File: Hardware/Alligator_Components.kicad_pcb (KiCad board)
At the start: 2 copper layers, 60 x 110 mm, 109 parts, among them J1 SWD_Header, J2 Eurorack_10_pin_power, J3 Conn_01x08_Female, J4 Conn_01x08_Female, J5 Conn_01x08_Female, J6 Conn_01x08_Female, U1 STM32H743ZITx, U2 IS42S16400J-xC, U3 PCM5100APW, U4 SSI2164, U5 MCP6004, U6 MCP6004, U7 TL074, U8 LM1117-3.3, Y1 8MHz 20pF

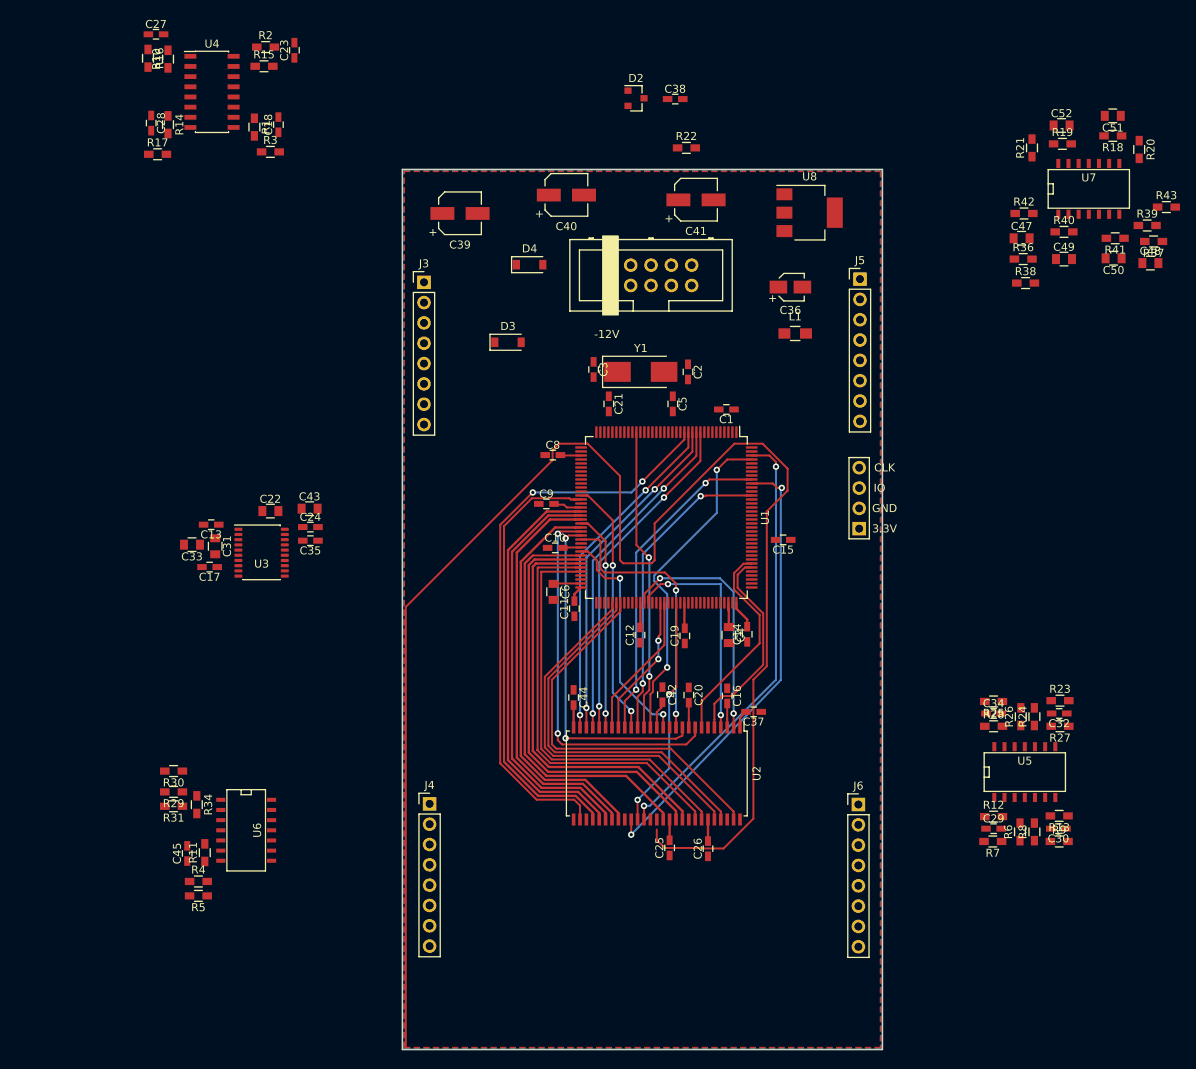
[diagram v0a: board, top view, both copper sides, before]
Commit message: Further routing of PCB
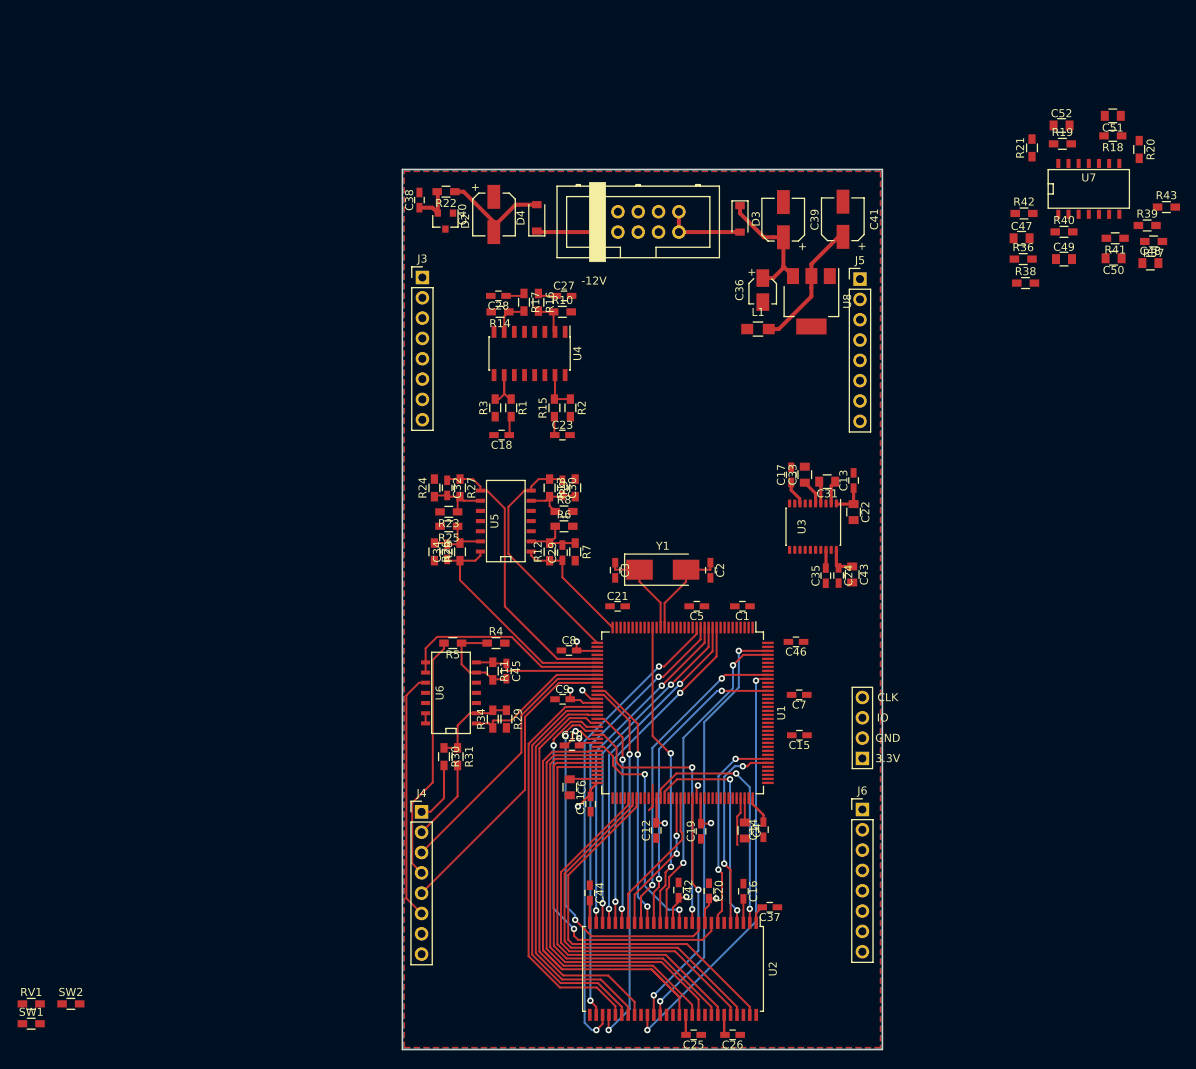
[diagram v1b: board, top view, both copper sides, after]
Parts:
- added C46: 100nF, Capacitors_SMD:C_0603_HandSoldering, F.Cu at (149.2, 109.0)
- added C7: 100nF, Capacitors_SMD:C_0603_HandSoldering, F.Cu at (149.6, 115.7)
- added RV1: A10k, Resistors_SMD:R_0603_HandSoldering, F.Cu at (53.6, 154.3)
- added SW1: SW_SPST, Resistors_SMD:R_0603_HandSoldering, F.Cu at (53.6, 156.8)
- added SW2: SW_SPDT_MSM, Resistors_SMD:R_0603_HandSoldering, F.Cu at (58.6, 154.3)
- moved C32 81.5 mm to (105.6, 89.8), turned to 270 degrees
- moved R27 80.7 mm to (107.2, 89.8), turned to 270 degrees
- moved C13 80.5 mm to (156.4, 88.9), turned to 90 degrees
- moved R24 80.3 mm to (104.0, 89.8)
- moved R23 80.0 mm to (105.8, 92.8), turned to 180 degrees
- moved C33 77.1 mm to (150.3, 88.2), turned to 90 degrees
- moved C31 76.9 mm to (153.1, 89.0), turned to 180 degrees
- moved R26 76.1 mm to (104.0, 97.8), turned to 270 degrees
- moved R13 75.8 mm to (118.4, 89.8), turned to 270 degrees
- moved C30 75.2 mm to (120.0, 89.8), turned to 270 degrees
- moved R9 74.9 mm to (121.6, 89.8), turned to 90 degrees
- moved C17 73.6 mm to (148.6, 88.2), turned to 90 degrees
- moved C22 72.9 mm to (156.4, 92.8), turned to 270 degrees
- moved U5 72.1 mm to (112.8, 94.0), turned to 90 degrees
- moved R25 71.5 mm to (105.8, 94.6)
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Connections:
- J3 pad 2: /MODE1 -> /EXT_AUDIO_IN_L
- J3 pad 3: /MODE2 -> /EXT_AUDIO_IN_R
- J3 pad 4: /USB_VBUS -> /RESET
- J3 pad 5: /USB_DM -> /DELAY_CV_L
- J3 pad 6: /USB_DP -> /DELAY_CV_R
- J4 pad 1: /EXT_AUDIO_IN_L -> /MIX_CV
- J4 pad 2: /EXT_AUDIO_IN_R -> /MIX_POT
- J4 pad 3: /RESET -> /FEEDBACK_POT
- J4 pad 4: /EXT_AUDIO_OUT_L -> /FEEDBACK_CV
- J4 pad 5: /EXT_AUDIO_OUT_R -> /DELAY_POT_L
- J5 pad 1: /DELAY_CV_L -> /EXT_AUDIO_OUT_L
- J5 pad 2: /DELAY_POT_L -> /EXT_AUDIO_OUT_R
- J5 pad 3: /DELAY_CV_R -> /DELAY_POT_R
- J5 pad 4: /DELAY_POT_R -> /ADC12_INP7_PA7
- J5 pad 5: /ADC12_INP7_PA7 -> /ADC12_INP14_PA2
- J5 pad 6: /ADC12_INP14_PA2 -> /MODE1
- J5 pad 7: GND -> /MODE2
- J5 pad 8: +3.3VA -> Net-(J5-Pad8)
- J6 pad 1: /MIX_POT -> /LED1
- J6 pad 2: /MIX_CV -> /LED2
- J6 pad 3: /FEEDBACK_CV -> /USB_VBUS
- J6 pad 4: /FEEDBACK_POT -> /USB_DM
- J6 pad 5: /LED1 -> /USB_DP
- J6 pad 6: /LED2 -> Net-(J6-Pad6)
- U1 pad 117: Net-(U1-Pad117) -> /DAC_BCLK
- U1 pad 27: /AUDIO_IN_R -> /MIX_WET_CTL
- U1 pad 29: Net-(U1-Pad29) -> /DAC_DATA
- U1 pad 34: /DELAY_CV_R -> /MIX_DRY_CTL
- U1 pad 36: Net-(U1-Pad36) -> /AUDIO_IN_L
- U1 pad 37: /DELAY_CV_SCALED_L -> /AUDIO_IN_R
- U1 pad 40: /MIX_DRY_CTL -> Net-(U1-Pad40)
- U1 pad 41: /MIX_WET_CTL -> /DELAY_CV_SCALED_L
- U1 pad 42: /AUDIO_IN_L -> /DELAY_CV_SCALED_R
- U1 pad 43: /FEEDBACK_CV_SCALED -> /CLOCK_SCALED
- U1 pad 44: /DELAY_CV_SCALED_R -> /FEEDBACK_CV_SCALED
- U1 pad 45: /DELAY_POT_L -> /WET_DRY_MIX
- U1 pad 47: /WET_DRY_MIX -> /DELAY_POT_L
- U1 pad 69: /DAC_BCLK -> Net-(U1-Pad69)
- U1 pad 76: /DAC_DATA -> Net-(U1-Pad76)
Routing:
- net (no net): track 195.2 -> 0.00 mm
- net /FMC_A5: track 0.00 -> 59.7 mm, vias 0 -> 2
- net /DELAY_POT_L: track 0.00 -> 38.2 mm
- net /DELAY_CV_SCALED_L: track 0.00 -> 35.6 mm
- net /FEEDBACK_POT: track 0.00 -> 33.7 mm
- net /CLOCK: track 0.00 -> 31.1 mm
- net /FEEDBACK_CV: track 0.00 -> 30.9 mm
- net +3V3: track 39.4 -> 70.1 mm, vias 0 -> 8
- net /AUDIO_IN_R: track 0.00 -> 30.2 mm
- net /DELAY_CV_SCALED_R: track 0.00 -> 29.2 mm
- net /CLOCK_SCALED: track 0.00 -> 26.6 mm
- net /WET_DRY_MIX: track 0.00 -> 18.6 mm
- net /FMC_A4: track 72.1 -> 54.9 mm
- net /FMC_D8: track 52.4 -> 69.2 mm
- net VCC: track 0.00 -> 16.2 mm
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- added copper zone on In2.Cu, net +3V3
- added copper zone on In1.Cu, net GND
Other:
- copper layers 2 -> 4
